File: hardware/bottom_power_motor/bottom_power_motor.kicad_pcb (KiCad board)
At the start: 4 copper layers, 52 x 52 mm, 81 parts, among them J1 Feld 16p, J2 J_STK_A, J3 J_STK_B, Q1 P-FET 40V 30A, U2 TPS54360, U2_CB 100n, U2_CO 47u, U2_CZ 3n3, U2_D 60V 3A, U2_L 10u, U2_RC 10k, U2_RH 53k6, U2_RL 10k2, U2_RT_R 100k, U3 TLV62569, U4 TPS54360, U4_CB 100n, U4_CO 22u, U4_CZ 3n3, U4_D 60V 3A, U4_L 33u, U4_RC 10k, U4_RH 68k1, U4_RL 10k0, U4_RT_R 100k

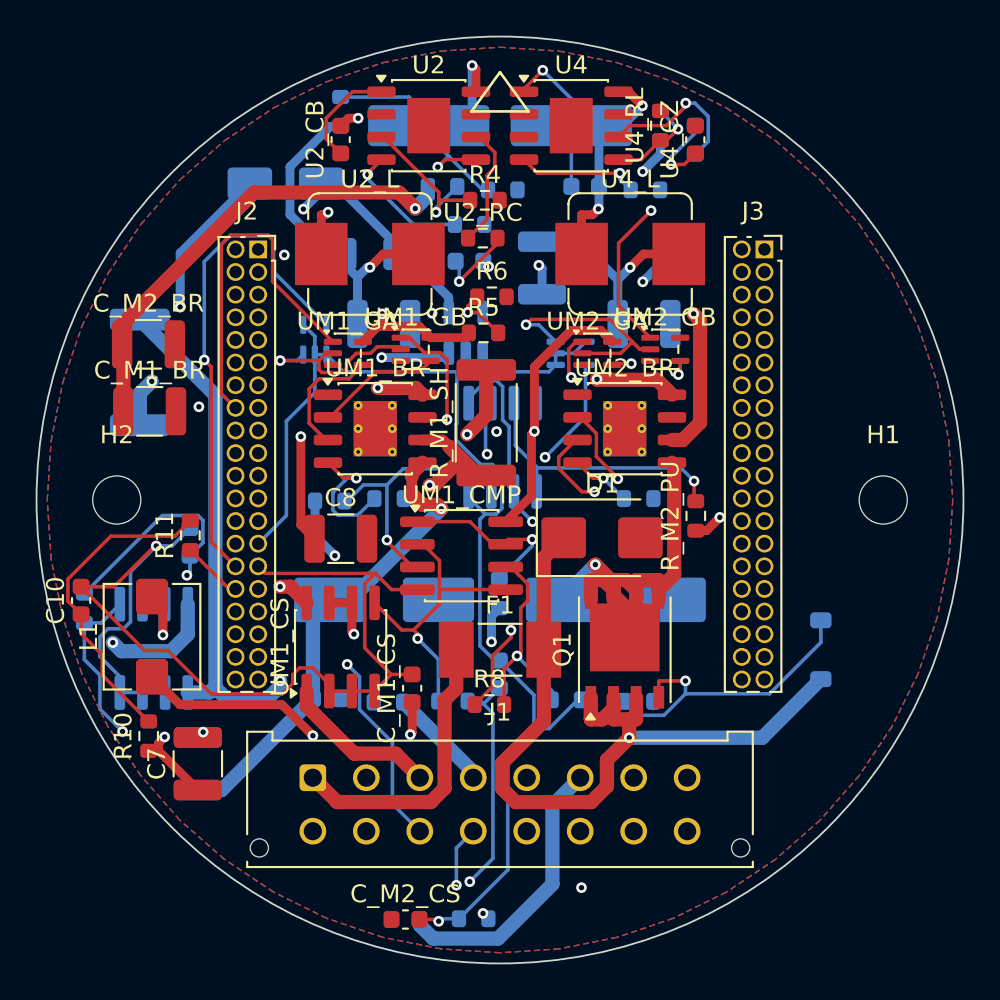
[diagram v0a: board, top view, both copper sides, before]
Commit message: Stackverbinder und FPC-Buchse auf die richtigen Seiten
DIE STACKVERBINDER SASSEN AUF ALLEN DREI BOARDS AUF DER VORDERSEITE. Drei
gleiche Buchsen auf drei Vorderseiten koennen nicht ineinandergreifen - das
war als Beschaffungsfrage bekannt (docs/06, Punkt 23), aber niemand hatte
gepruefte, was es fuer die Platzierung bedeutet.

Auf Top stand die Buchse genau dort, wo das Displaypanel aufliegen soll:
8 mm hoch, mitten unter der Klebeflaeche. Das Panel haette nirgends
aufliegen koennen.

Der Koerper gehoert jeweils auf die Seite, die zum naechsten Board zeigt:

  Bottom  F traegt den Feldstecker und zeigt in den Kabelraum -> B
  Mid     F zeigt zu Top, dort steht auch die USB-Buchse      -> F
  Top     B zeigt zu Mid, Vorderseite bleibt fuers Panel      -> B

Mid braucht damit einen echten STAPELverbinder: Buchse auf der einen Seite,
lange Stifte auf der anderen. Das ist Punkt 23, und daran haengt auch der
Plattenabstand.

J5 IST EBENFALLS AUF DIE RUECKSEITE GEWANDERT. Eine FPC-Buchse von 1,2 mm
Hoehe unter einem aufgeklebten Panel geht nicht. Die Fahne ist 18,15 mm lang
und laut Zeichnung ohnehin gefaltet - sie greift um die Boardkante.

Alle drei Boards platzieren fehlerfrei. Im Panelbereich steht vorn nur noch
die Klinkenbuchse - und die passt dort nicht mehr hin, siehe naechster
Commit.

Co-Authored-By: Claude Opus 5 (1M context) <noreply@anthropic.com>
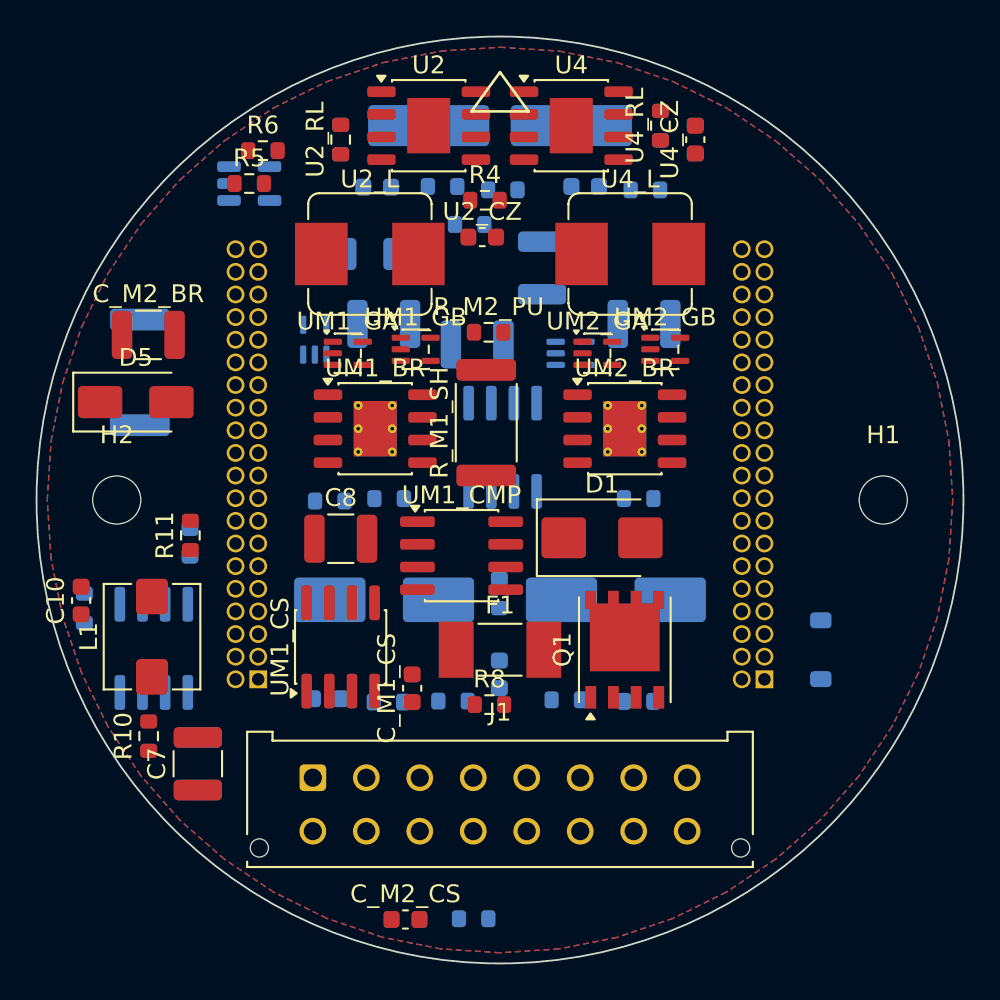
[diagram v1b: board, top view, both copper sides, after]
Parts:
- C_M1_BR, J2, J3, U2_CB, U2_RC: moved to B.Cu
- D5, U2_CZ, U2_RL: moved to F.Cu
- moved J2 24.1 mm to (-13.6, 10.1)
- moved J3 24.1 mm to (14.8, 10.1)
- moved C_M1_BR 18.8 mm to (-1.28, -8.73)
- moved R5 15.6 mm to (-14.1, -17.8)
- moved R_M2_PU 15.5 mm to (-0.64, -9.41), turned to 0 degrees
- moved R6 15.2 mm to (-13.3, -19.6)
- moved D5 14.9 mm to (-20.4, -5.49)
- moved U3 14.8 mm to (-14.1, -17.8), turned to 0 degrees
- moved U2_RL 9.52 mm to (-8.94, -20.2), turned to 90 degrees
- moved U2_CB 3.36 mm to (-6.89, -17.6), turned to 0 degrees
- moved U2_RT_R 2.69 mm to (0.16, -17.4)
- moved U2_RH 1.56 mm to (-8.94, -20.2)
- moved U2_CZ 1.53 mm to (-1.00, -14.7)
- moved U2_RC 1.06 mm to (-1.70, -15.5)
- moved C_M2_BR 0.53 mm to (-19.7, -9.26)
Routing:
- net 3V3_SYS: track 142.6 -> 0.00 mm, vias 9 -> 0
- net AGND: track 134.9 -> 0.00 mm, vias 2 -> 0
- net 24V_PROT: track 104.2 -> 0.00 mm, vias 3 -> 0
- net M2_ISNS: track 72.8 -> 0.00 mm, vias 3 -> 0
- net M2_SWA: track 72.4 -> 0.00 mm, vias 3 -> 0
- net M2_INB: track 52.5 -> 0.00 mm, vias 1 -> 0
- net I_SENSE1: track 46.0 -> 0.00 mm, vias 1 -> 0
- net 24V_F: track 45.0 -> 0.00 mm, vias 1 -> 0
- net M2_A: track 44.7 -> 0.00 mm, vias 1 -> 0
- net M2_B: track 43.3 -> 0.00 mm, vias 1 -> 0
- net M2_INA: track 39.2 -> 0.00 mm, vias 3 -> 0
- net RS485_A: track 39.0 -> 0.00 mm
- net REED2_IN: track 38.3 -> 0.00 mm, vias 1 -> 0
- net M1_B: track 37.9 -> 0.00 mm, vias 2 -> 0
- net 5V_SYS: track 37.6 -> 0.00 mm, vias 2 -> 0
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
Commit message: Alle drei Boards kupferfehlerfrei, und die Bilder zeigen endlich die Stecker
ROUTING. Alle drei Platinen haben jetzt null Kupferfehler:

  Top     179 Segmente,  22 Vias,  7 Signale offen  (vorher 11, 2 Fehler)
  Mid     720 Segmente,  74 Vias,  4 Signale offen  (vorher  6)
  Bottom  811 Segmente,  91 Vias,  6 Signale offen  (vorher  8, 6 Fehler)

Top hatte zwei copper_edge_clearance-Fehler an der USB-C-Kerbe: Eine
BTN2-Bahn lief auf In1.Cu quer durch den Ausschnitt. Der Randkeepout des
Routers kannte die Kerbe gar nicht - er bestand aus vier Balken entlang der
Kanten, und die Kerbe schneidet in eine dieser Kanten hinein. Die einzige
Aussparung darin stammte noch von der Klinkenbuchse, die es nicht mehr gibt.
route_boards.py setzt jetzt NOTCH_KEEPOUT.

M1_ISNS AUF BOTTOM IST MIT ABSICHT LEER. Freerouting hatte das analoge
Motorstrom-Messsignal auf F.Cu direkt an die Vergleichsschwelle V_TRIP_LO
gepresst - vier Kurzschluesse, eine Kreuzung, ein Abstandsfehler, alle in
einem Feld von zwei Millimetern. Einzeln herausgeloeste Segmente haben das
Problem nur verschoben: nach jedem Eingriff dieselben zwei Netze an der
naechsten Stelle. Das Netz ist deshalb komplett entfernt und wird von Hand
gezogen. Sachlich ist die Paarung ohnehin die schlechteste denkbare - koppeln
Messsignal und Ausloeseschwelle, verstimmt sich die Hinderniserkennung
selbst, ohne dass eine DRC das je bemerkt. docs/16 erklaert es samt Auflagen.

DIE BILDER ZEIGTEN DIE STECKVERBINDER NICHT - und es lag nicht an den
Modellen. Die Bildkette war nie ein Skript, sondern jedes Mal von Hand
getippt. Dadurch stammten die Teile aus verschiedenen Zeitpunkten: Modelle
16:04, Stapel-STEPs 15:59, Unterseiten-Renderings 13:41. Ausgerechnet die
Unterseiten zeigen den Feldstecker und die USB-Buchse.

tools/render_all.py macht daraus einen Aufruf: sechs Boardansichten, drei
STEP-Ausgaben mit Modellen, das Stapelbild und die Gesamtbaugruppe - ein
Zeitstand fuer alles. Renderings jetzt mit transparentem Hintergrund, damit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
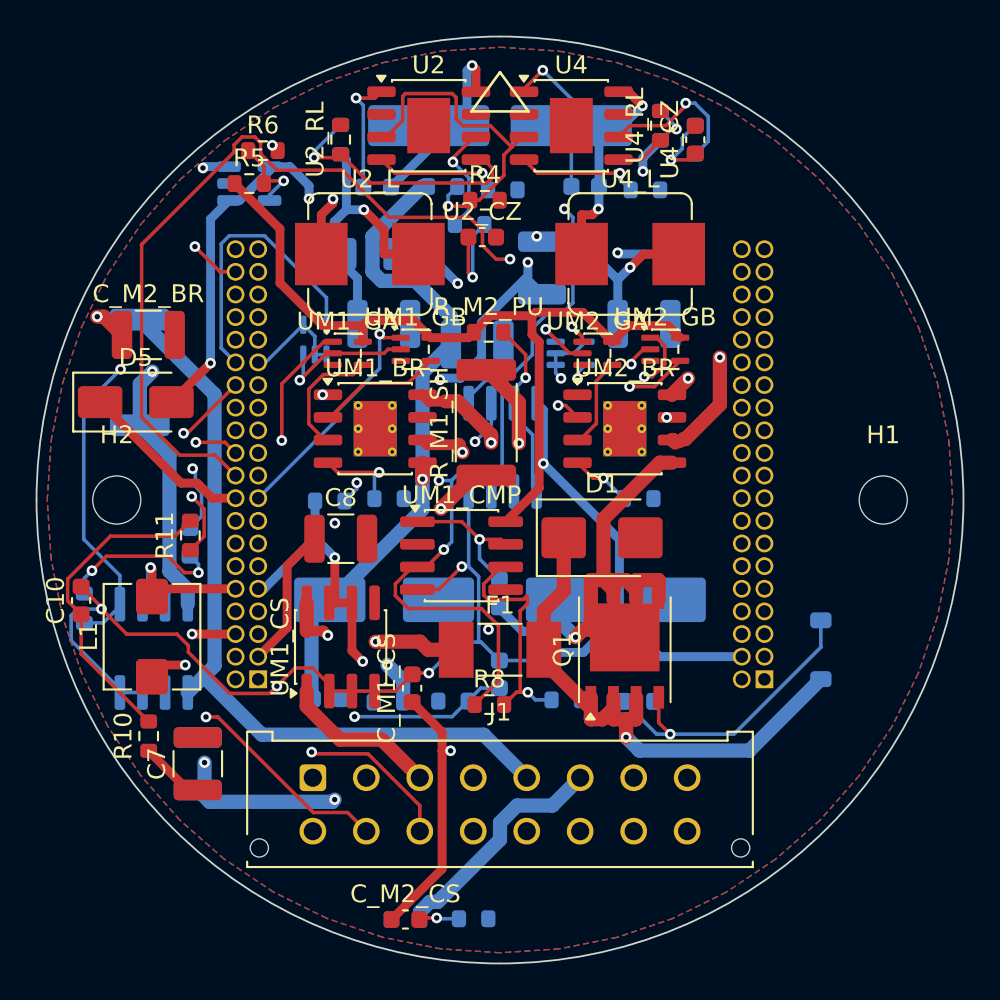
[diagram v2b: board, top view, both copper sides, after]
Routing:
- net 3V3_SYS: track 0.00 -> 147.8 mm, vias 0 -> 5
- net 24V_PROT: track 0.00 -> 142.6 mm, vias 0 -> 5
- net AGND: track 0.00 -> 134.6 mm, vias 0 -> 7
- net 5V_SYS: track 0.00 -> 71.4 mm, vias 0 -> 4
- net M2_ISNS: track 0.00 -> 70.9 mm, vias 0 -> 2
- net HOOD_A: track 0.00 -> 69.9 mm, vias 0 -> 1
- net M2_SWA: track 0.00 -> 62.3 mm, vias 0 -> 2
- net RS485_A: track 0.00 -> 60.7 mm
- net M2_INA: track 0.00 -> 49.7 mm, vias 0 -> 2
- net HOOD_B: track 0.00 -> 47.2 mm
- net M2_INB: track 0.00 -> 47.1 mm, vias 0 -> 2
- net M2_A: track 0.00 -> 43.7 mm
- net M2_B: track 0.00 -> 39.3 mm, vias 0 -> 1
- net M1_INA: track 0.00 -> 37.6 mm, vias 0 -> 1
- net SAB1_IN: track 0.00 -> 36.9 mm, vias 0 -> 1
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
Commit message: Hauptschalter, Magnetkontakt im Rahmen, verschraubter Stapel - Umbau v0.7
VIER ENTSCHEIDUNGEN VOM 19.08.2026, alle umgesetzt:

1. HAUPTSCHALTER. Bisher stand nach dem Verschrauben von Bottom und Mid
sofort 24 V auf allem - ohne dass das Top-Board steckte. Jetzt laeuft der
Gate-Pulldown des Verpolschutz-FETs als SCHLEIFE durch den Stapel:
Q1-Gate -> R1 -> EN_LOOP (Stapelkontakt B2, war PGND; Pinout v0.7) -> SW5
auf Top -> PGND. Neuer 1-M-Pullup R1B haelt das Gate bei offener Schleife
definiert an der Source. Top-Board fehlt ODER SW5 aus -> Q1 sperrt, nichts
bekommt 24 V. Der Schalter traegt nur den Teilerstrom (~20 uA).
SW5 ist ein Copal CVS-01 (1,5 mm hoch, unter der Scheibe, durch eine
Oeffnung bedienbar). Er sitzt HOCHKANT bei (11,9/-19,4): Das Fenster
zwischen ToF-Courtyard (bis 8,245) und Ecktaster (ab 15,205) ist 6,96 mm
breit, der Schalter waagerecht 7,69 - drei Anlaeufe bei 12,5, 11,0 und 11,9
endeten in DRC-Ueberlappungen, erst das Ausmessen statt Schaetzens der
Courtyards zeigte, dass NUR gedreht Platz ist.

2. MAGNETKONTAKT IN DEN ABDECKRAHMEN, unten mittig - dort haelt auch das
vorhandene DCX-909 (Gewinde OD 8, im Rahmen ist Platz; Messpunkt F14: ist
der Rahmen dort hohl?). Das Magnetlangloch im Top-Board (Zwischenloesung
von einem Tag) ist wieder raus, mit ihm die 6,8-mm-Grenze, an der jedes
Kaufteil scheiterte. Neu: KABELKERBE 5 x 2 unten mittig, J6 dahinter
mittig auf der Rueckseite. Router-Keepout entsprechend getauscht.

3. LOETSCHEIBE hardware/stern_puck/ (OE 16, zweilagig, DRC null Fehler):
verbindet die Steckseite des DCX-909 mit den Litzen des Sterns. Litzen
durch Fesselbohrungen faedeln, umschlagen, loeten - die Zugentlastung ist
die Bohrung, nicht das Zinn. Drei eigene DRC-Runden gebraucht: 2,0er Pads
beruehren sich bei 1,85 Stiftabstand, die Minus-Bruecke lief durch das
Plus-Pad, die Fesselbohrungen brauchten seitliche Lage und OE 16 statt 14.

4. BEFESTIGUNGSKONZEPT v2 (docs/04, 2b): verschraubt statt nur gesteckt.
NEU mechanical/tragring.py 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
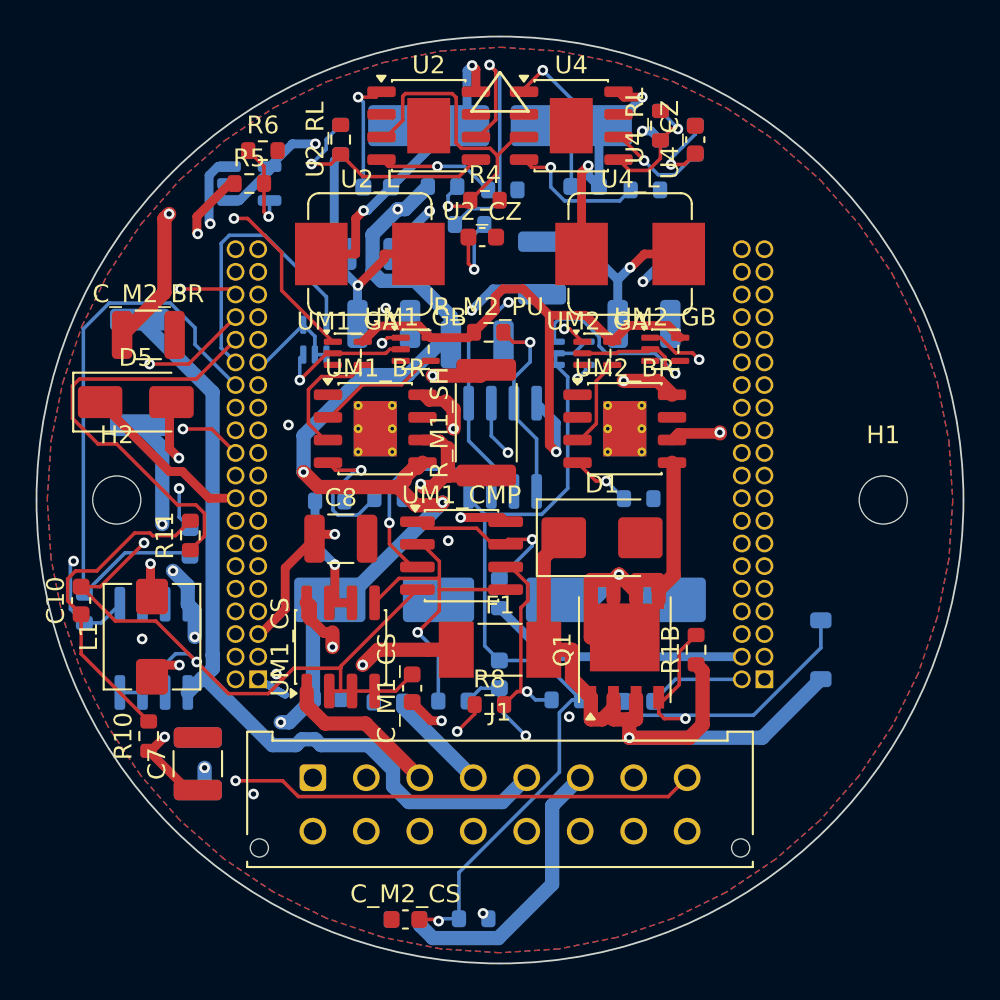
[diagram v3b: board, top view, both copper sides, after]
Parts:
- added R1B: 1M, R_0603_1608Metric, F.Cu at (11.0, 8.40)
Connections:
- J3 pad 2: PGND -> EN_LOOP
- R1 pad 2: PGND -> EN_LOOP
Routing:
- net I_SENSE1: track 33.5 -> 66.2 mm, vias 1 -> 2
- net HOOD_A: track 69.9 -> 46.8 mm
- net M1_ISNS: track 0.00 -> 18.4 mm, vias 0 -> 1
- net 3V3_SYS: track 147.8 -> 160.8 mm, vias 5 -> 8
- net M2_INA: track 49.7 -> 37.2 mm, vias 2 -> 1
- net 6V2_STAR_F: track 34.4 -> 45.0 mm, vias 4 -> 2
- net TRIP_RST: track 13.4 -> 24.0 mm, vias 1 -> 0
- net REED1_IN: track 36.0 -> 46.2 mm, vias 1 -> 2
- net I_SENSE2: track 23.2 -> 33.4 mm, vias 3 -> 0
- net U2_COMP: track 6.21 -> 15.6 mm
- net M2_GB: track 9.25 -> 0.00 mm, vias 2 -> 0
- net HOOD_B: track 47.2 -> 56.0 mm
- net U2_SW: track 25.0 -> 17.4 mm
- net M2_SWA: track 62.3 -> 54.8 mm, vias 2 -> 4
- net 24V_F: track 31.5 -> 39.0 mm
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
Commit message: Leistungsvias, Via-Strompruefung, Reset/Boot-Durchgriffe und der Gehaeusebecher
VIER ARBEITEN AUS EINEM ABEND, alle aus Rueckfragen entstanden:

1. VIAS SIND NICHT BELIEBIG STROMTRAGFAEHIG - der Einwand traf: 24V_IN
lief ueber genau EIN 0,6/0,3-Via (~1,2 A) bei 4,1 A Grenzstrom, dazu 14
weitere Engpaesse auf Bottom. Ursache: Die Bottom-Klassen routeten mit dem
Standardvia - ein Erbe der diskreten H-Bruecke, zwischen deren FETs das
0,8er nicht passte; Mid und Top hatten das Leistungsvia laengst. Jetzt:
PWR- und RAIL-Klasse auf Bottom mit 0,8/0,4, Massebruecken dort ebenso
(deren Platzsuche folgt jetzt der Viagroesse - die alte 0,6er-Suche setzte
0,8er-Vias in 0,6er-Luecken, vier Abstandsfehler).

NEU tools/via_check.py: prueft nach jedem Routing jedes Via gegen den
Dauerstrom seines Netzes (4 A je mm Bohrung, 3-mm-Parallelgruppen);
--fix setzt Zwillingsvias. Zwei eigene Fehler auf dem Weg, beide vom
Werkzeug selbst aufgedeckt: KiCad-10-Formabfragen brauchen eine Lage, und
die erste Freiraumpruefung sah nur F/B - ein Via bohrt aber durch ALLE
vier Lagen; 15 Innenlagen-Kurzschluesse, alle rueckstandslos entfernt.
Endstand: 27 Zwillinge gesetzt, 11 dokumentierte Engpaesse als
Handarbeitsliste mit Koordinaten in docs/16.

2. RESET UND BOOT WAREN UNERREICHBAR - SW1 sass mitten unter dem
Top-Board, SW2 zeigte zur Rueckseite. Beide jetzt auf Mids Vorderseite bei
(+-8/18,6), darueber zwei OE-3,2-Durchgriffe H3/H4 im Top-Board: Scheibe
ab, Stift durch, druecken. Im Betrieb verdeckt die Scheibe die Loecher.

3. DER GEHAEUSEBECHER (mechanical/gehaeuse.py): kapselt Bottom und Mid,
Rueckwand mit Tunnelfenster fuer die Feldstecker-Leiste - sie bleibt als
einziges von hinten zugaenglich. Verbindung zum Tragring per BAJONETT:
drei Zapfen an 12/3/9 Uhr, ~7 Grad Drehung, tangential auskragende
Koepfe - radiale Rasthaken scheiterten dreifach (Adapter auf den
Diagonalen, Dosenwand aussen, Adapterbasis innen; frei ist nur ein
2,2-mm-Band auf den Achsen). Wand an den Schraubdomen gefenste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
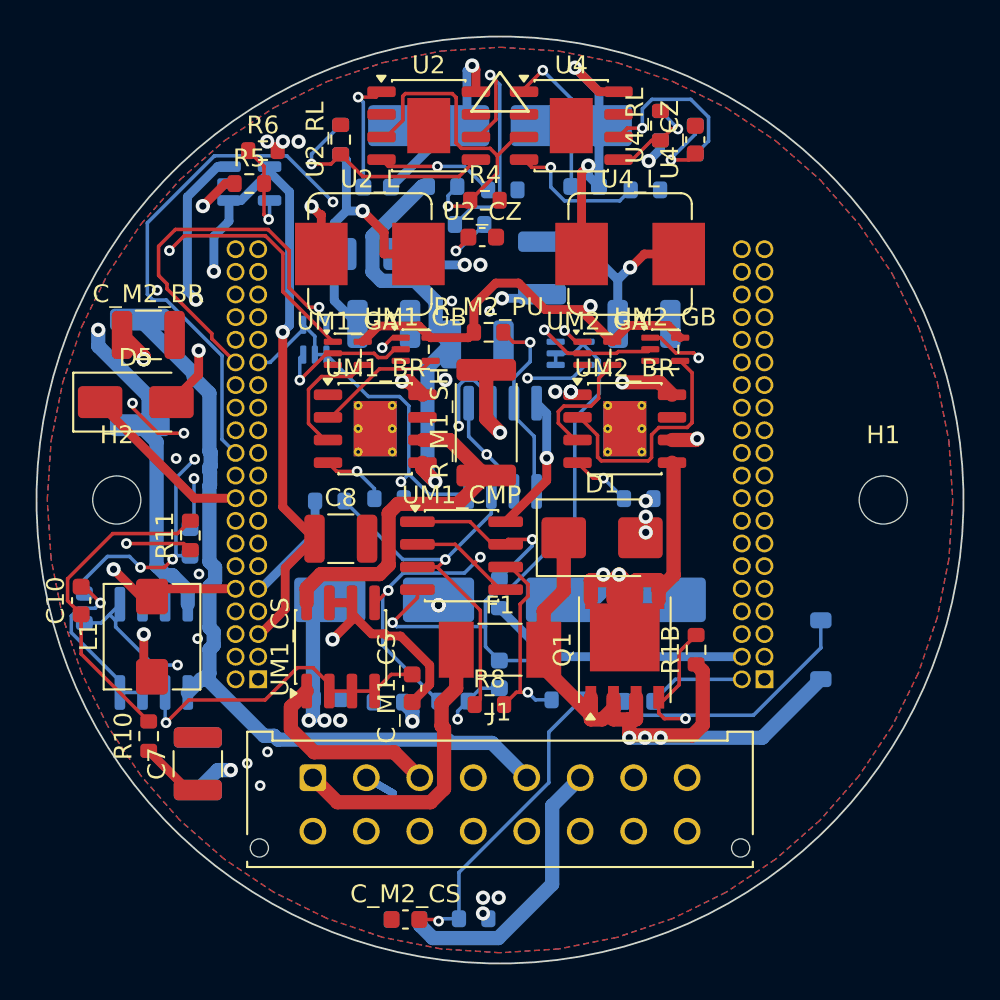
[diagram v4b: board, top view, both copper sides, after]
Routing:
- net I_SENSE1: track 66.2 -> 36.5 mm, vias 2 -> 3
- net M2_ISNS: track 66.2 -> 40.2 mm
- net 6V2_STAR_F: track 45.0 -> 23.8 mm, vias 2 -> 1
- net 24V_PROT: track 135.7 -> 116.7 mm, vias 7 -> 9
- net I_SENSE2: track 33.4 -> 18.7 mm, vias 0 -> 3
- net V_TRIP_HI: track 36.9 -> 22.5 mm, vias 2 -> 1
- net M2_GB: track 0.00 -> 13.5 mm
- net HOOD_B: track 56.0 -> 43.6 mm
- net AGND: track 140.2 -> 151.6 mm, vias 5 -> 6
- net U2_SW: track 17.4 -> 26.0 mm
- net M2_SWA: track 54.8 -> 63.0 mm, vias 4 -> 2
- net HOOD_A: track 46.8 -> 55.0 mm, vias 1 -> 0
- net M2_SD: track 15.6 -> 7.52 mm
- net RS485_A: track 61.9 -> 54.1 mm
- net REED1_IN: track 46.2 -> 40.3 mm, vias 2 -> 0
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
